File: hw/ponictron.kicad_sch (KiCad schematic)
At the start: 80 parts, among them IC1 SHT40-BD1B-R2, IC2 MAX31328NELB+, IC3 PEC11S-929K-S0015, J1 RJCSE538001, J10 B3B-PH-SM4-TB_LF__SN_, J11 470531000, J12 SM04B-SRSS-TB_LF__SN__P_, J13 FC68148S, J2 Conn_01x10, J3 MSD-11-A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

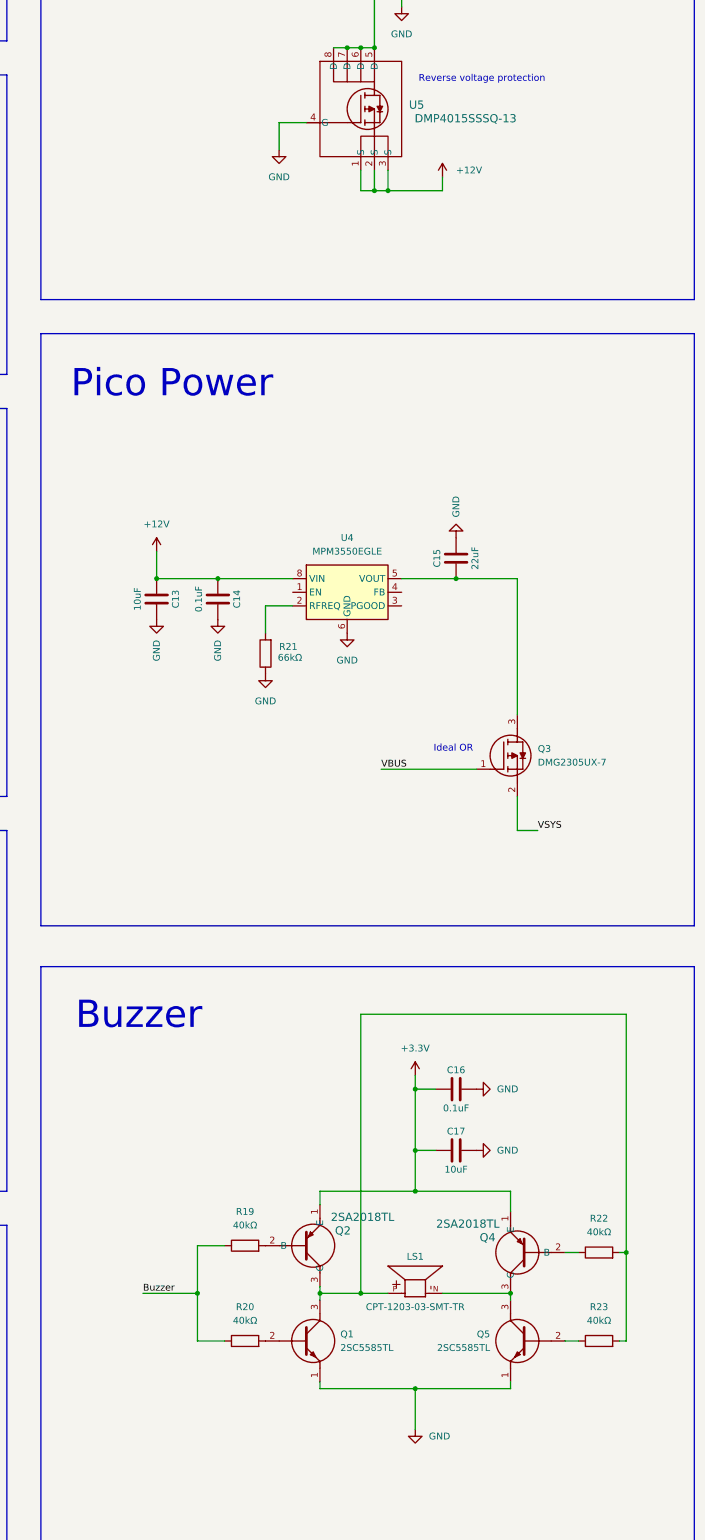
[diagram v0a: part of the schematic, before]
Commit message: Making changes to schematic based on feedback
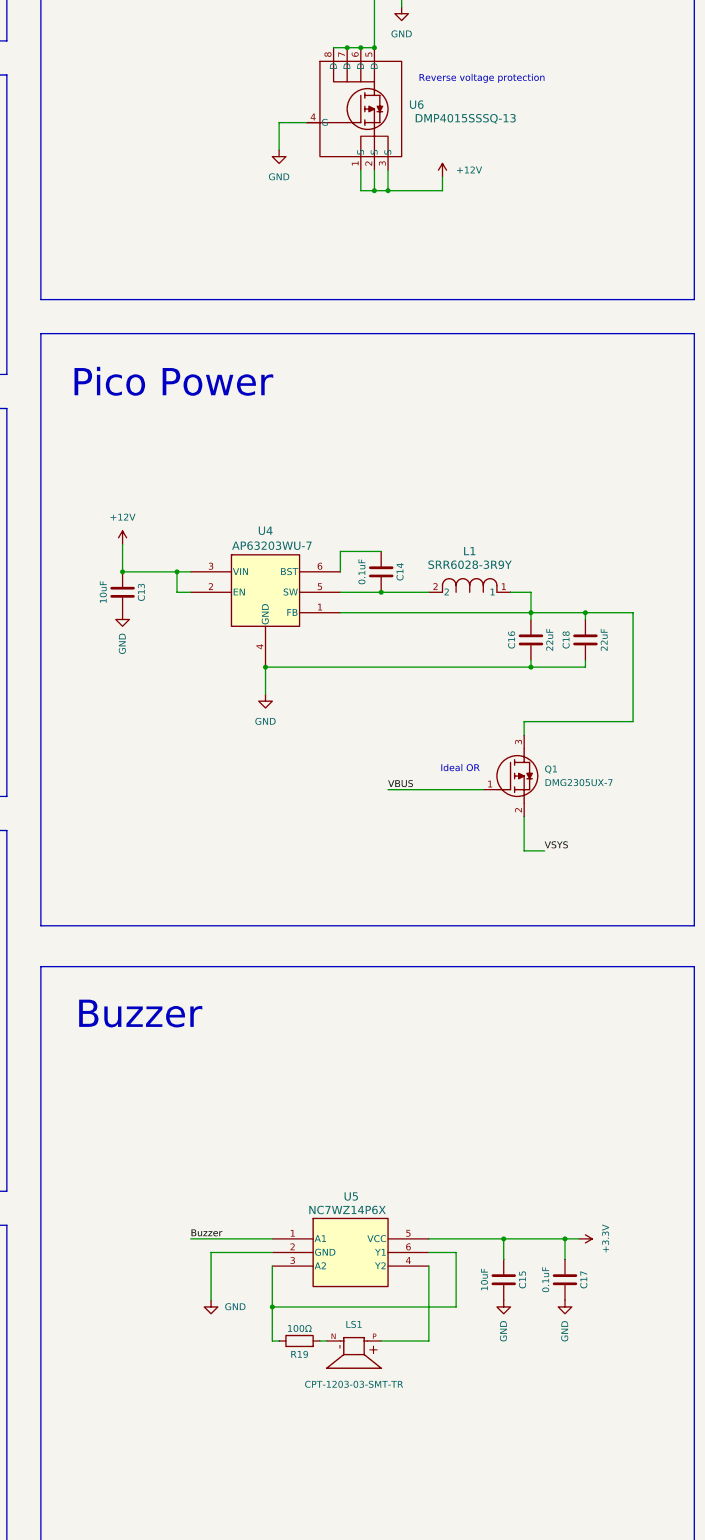
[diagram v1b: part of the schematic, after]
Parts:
- removed Q1, Q5: 2SC5585TL, SamacSys_Parts:2SC5585TL, symbol SamacSys_Parts:2SC5585TL
- removed Q2, Q4: 2SA2018TL, TRANS_2SA2018_ROM, symbol 2SA2018TL:2SA2018TL
- removed R20, R22, R23: 40kΩ, Resistor_SMD:R_0603_1608Metric_Pad0.98x0.95mm_HandSolder, symbol Device:R
- removed R21: 66kΩ, Resistor_SMD:R_0603_1608Metric_Pad0.98x0.95mm_HandSolder, symbol Device:R
- removed U4: MPM3550EGLE, MPM3550EGLE:MPM3550EGLE, symbol Regulator_Switching:MPM3550EGLE
- added C18: 22uF, Capacitor_SMD:C_0603_1608Metric, symbol Device:C
- added L1: SRR6028-3R9Y, IND_BOURNS_SRR6028, symbol SRR6028-3R9Y:SRR6028-3R9Y
- added U4: AP63203WU-7, AP63203WU-7_DIO, symbol AP63203WU-7:AP63203WU-7
- added U5: NC7WZ14P6X, SC70-6_ONS, symbol NC7WZ14P6X:NC7WZ14P6X
- R19: value 40kΩ -> 100Ω; LCSC Part # C100819 -> C15401
- renumbered C17 to C15, C15 to C16, C16 to C17, Q3 to Q1, U5 to U6
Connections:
- net +12V: now also U4.2 (EN), U4.3 (VIN); no longer C14.2
- net +3.3V: now also U5.5 (VCC)
- net Buzzer: now also U5.1 (A1); no longer R19.1
- net GND: now also C16.2, C18.2, U4.4 (GND), U5.2 (GND); no longer C14.1, C16.1
- net at Q1.3 (D): now also C16.1, C18.1, L1.1, U4.1 (FB); no longer C16.2
- net at LS1.P: now also U5.4 (Y2)
- net at LS1.N: now also R19.2
- new net: C14.1, L1.2, U4.5 (SW)
- new net: C14.2, U4.6 (BST)
- new net: R19.1, U5.3 (A2), U5.6 (Y1)
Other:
- moved on the sheet: C13, C14, C15, C16, C17, LS1, Q1

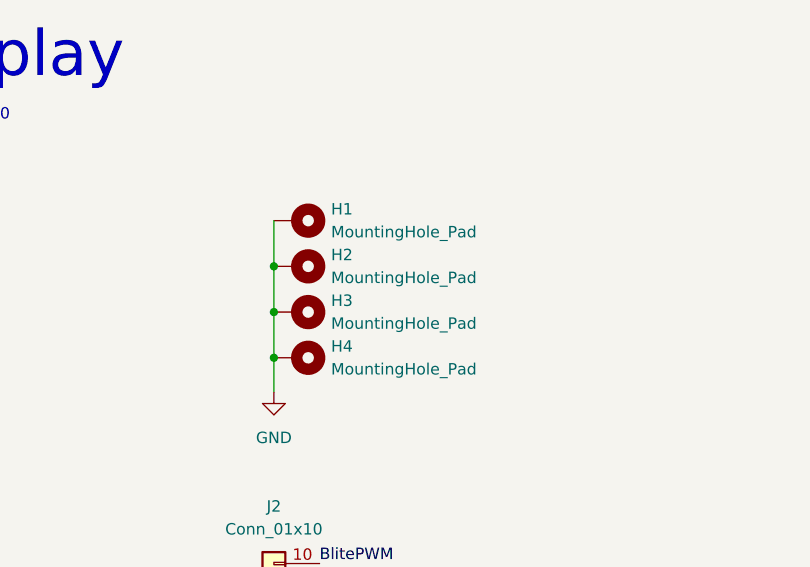
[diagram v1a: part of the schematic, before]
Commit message: Change display thru-holes to insert mounts
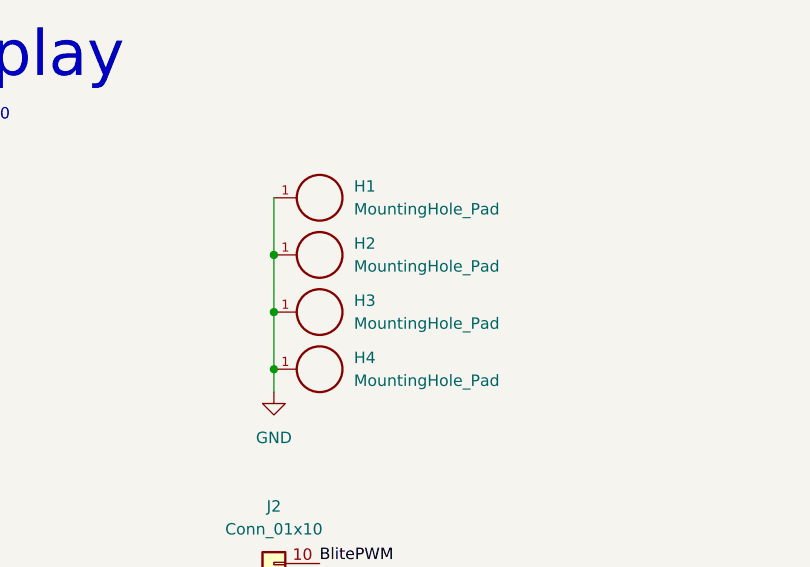
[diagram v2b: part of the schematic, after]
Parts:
- H1, H2, H3, H4: footprint MountingHole:MountingHole_2.7mm_M2.5_DIN965_Pad -> 78614015360:WE-SMSA_78614015360; symbol Mechanical:MountingHole_Pad -> 78614015360:WE-SMSA_M3; now in the parts list
